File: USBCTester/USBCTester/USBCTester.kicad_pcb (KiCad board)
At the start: 4 copper layers, 114.9 x 92.1 mm, 64 parts, among them J1 AUSB1-DFN-PTR3, J2 AUSB1-DFN-PTR3, SW1 SW_Push, U1 74HC595, U2 74HC595, U3 74HC595, U4 74HC595, U5 74HC595, U6 74HC595, U7 RaspberryPi_Pico

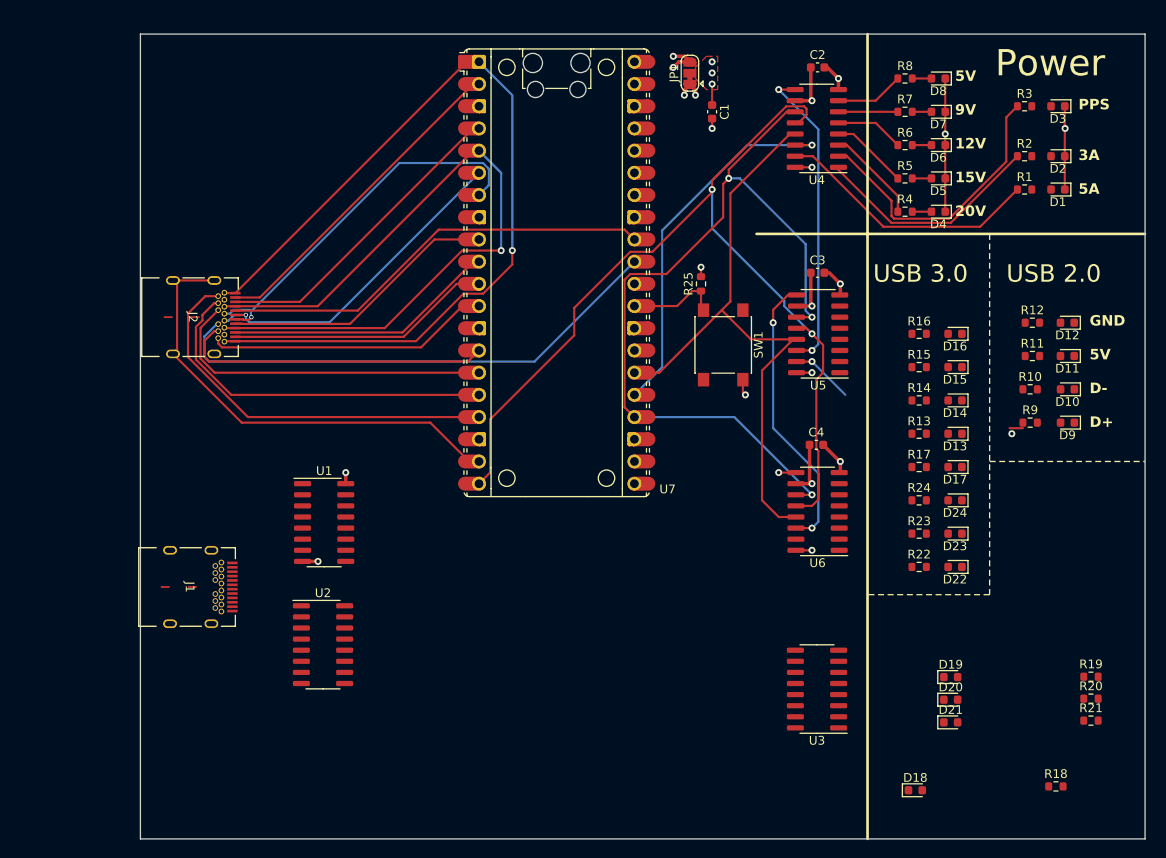
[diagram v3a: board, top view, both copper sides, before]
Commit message: add more leds and route almost everything
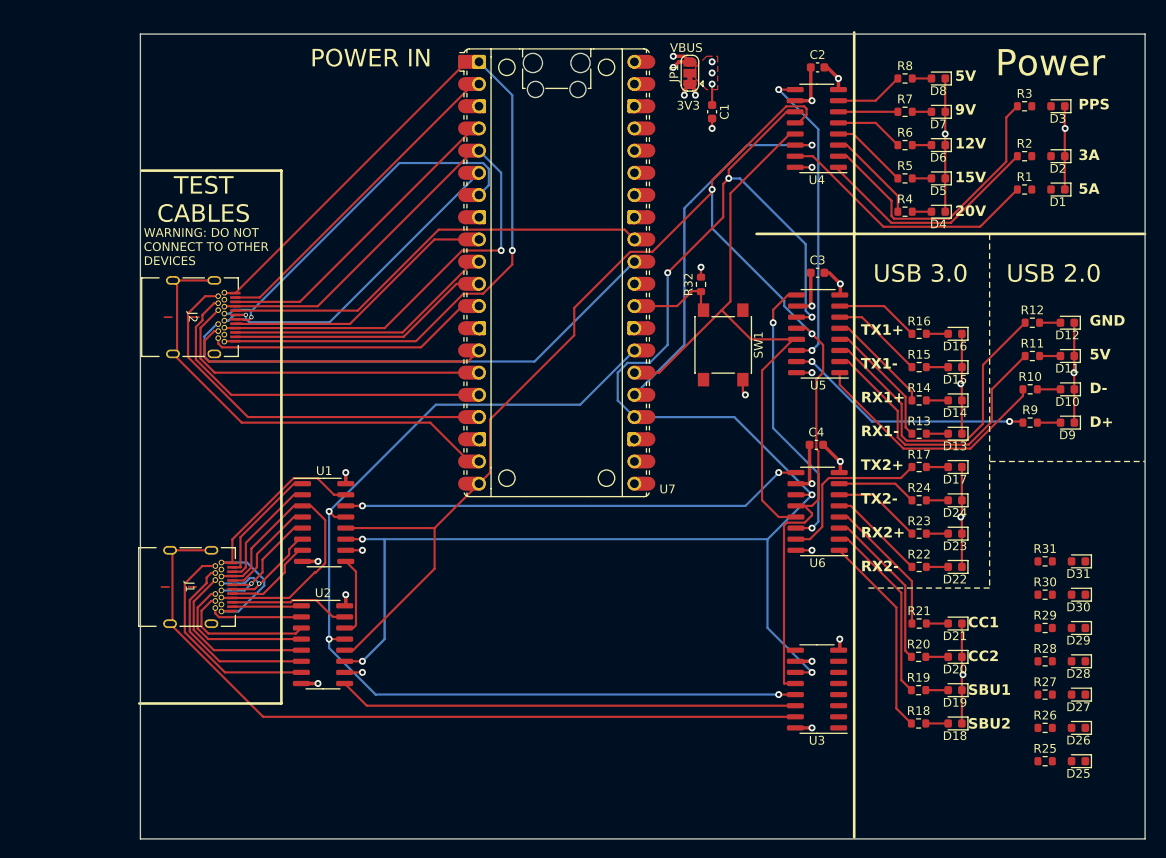
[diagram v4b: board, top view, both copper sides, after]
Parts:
- added D25: LED, LED_SMD:LED_0603_1608Metric, F.Cu at (212.1, 144.8)
- added D26: LED, LED_SMD:LED_0603_1608Metric, F.Cu at (212.1, 141.0)
- added D27: LED, LED_SMD:LED_0603_1608Metric, F.Cu at (212.1, 137.2)
- added D28: LED, LED_SMD:LED_0603_1608Metric, F.Cu at (212.1, 133.3)
- added D29: LED, LED_SMD:LED_0603_1608Metric, F.Cu at (212.1, 129.5)
- added D30: LED, LED_SMD:LED_0603_1608Metric, F.Cu at (212.1, 125.7)
- added D31: LED, LED_SMD:LED_0603_1608Metric, F.Cu at (212.1, 121.9)
- added R26: R, Resistor_SMD:R_0603_1608Metric, F.Cu at (208.3, 141.0)
- added R27: R, Resistor_SMD:R_0603_1608Metric, F.Cu at (208.3, 137.2)
- added R28: R, Resistor_SMD:R_0603_1608Metric, F.Cu at (208.3, 133.3)
- added R29: R, Resistor_SMD:R_0603_1608Metric, F.Cu at (208.3, 129.5)
- added R30: R, Resistor_SMD:R_0603_1608Metric, F.Cu at (208.3, 125.7)
- added R31: R, Resistor_SMD:R_0603_1608Metric, F.Cu at (208.3, 121.9)
- added R32: R, Resistor_SMD:R_0603_1608Metric, F.Cu at (168.9, 90.2)
- moved R25 67.3 mm to (208.3, 144.8), turned to 0 degrees
- moved R21 22.6 mm to (193.9, 129.0)
- moved R20 20.3 mm to (193.8, 132.8)
- moved R19 19.8 mm to (193.8, 136.7)
- moved R18 17.3 mm to (193.8, 140.5)
- moved D21 11.3 mm to (198.0, 129.0), turned to 180 degrees
- moved D18 8.89 mm to (198.0, 140.5), turned to 180 degrees
- moved D20 4.93 mm to (198.0, 132.8), turned to 180 degrees
- moved D19 1.57 mm to (198.0, 136.7), turned to 180 degrees
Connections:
- R25 pad 1: Net-(U7-GPIO22) -> Net-(U3-QB)
- R25 pad 2: GND -> Net-(D25-A)
- U3 pad 1: Net-(J5-Pin_2) -> Net-(U3-QB)
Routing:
- net Net-(U1-~{OE}): track 0.00 -> 117.7 mm, vias 0 -> 3
- net SRCLK: track 94.7 -> 186.3 mm, vias 3 -> 7
- net Net-(U3-QA): track 0.00 -> 89.3 mm
- net RCLK: track 110.4 -> 172.0 mm
- net Net-(U2-QH'): track 0.00 -> 52.6 mm
- net Net-(U1-SER): track 1.97 -> 53.1 mm, vias 1 -> 2
- net GND: track 39.9 -> 89.2 mm, vias 8 -> 14
- net Net-(U5-QD): track 0.00 -> 37.2 mm
- net TEST_CABLE_VBUS: track 0.00 -> 35.6 mm
- net TEST_CABLE_GROUND: track 0.00 -> 34.4 mm
- net Net-(U5-QC): track 0.00 -> 33.3 mm
- net Net-(U5-QB): track 0.00 -> 28.6 mm
- net Net-(U2-QH): track 0.00 -> 25.1 mm
- net Net-(U6-QB): track 0.00 -> 23.2 mm
- net Net-(U2-QG): track 0.00 -> 22.4 mm
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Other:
- board text added: "3V3"
- board text added: "CC1 CC2 SBU1 SBU2"
- board text added: "POWER IN"
- board text added: "TEST CABLES"
- board text added: "TX1+ TX1- RX1+ RX1- TX2+ TX2- RX2+ RX2-"
- board text added: "VBUS"
- board text added: "WARNING: DO NOT CONNECT TO OTHER DEVICES"

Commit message: label all LEDs
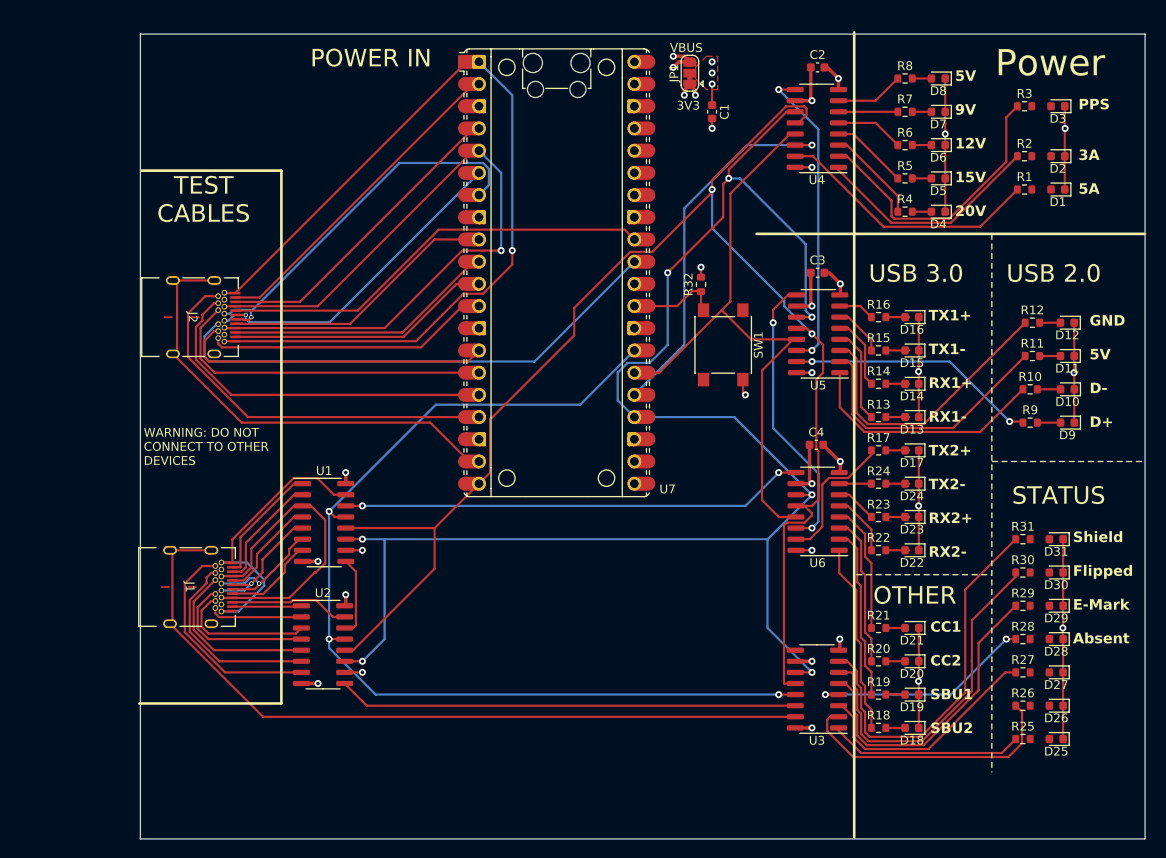
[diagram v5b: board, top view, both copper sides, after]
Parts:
- moved D13 5.28 mm to (193.0, 105.4)
- moved D14 5.28 mm to (193.0, 101.6)
- moved D16 5.28 mm to (193.0, 94.0)
- moved D17 5.28 mm to (193.0, 109.2)
- moved D22 5.28 mm to (193.0, 120.7)
- moved D23 5.28 mm to (193.0, 116.8)
- moved D24 5.28 mm to (193.0, 113.0)
- moved D15 5.28 mm to (193.0, 97.8)
- moved R13 5.01 mm to (189.2, 105.4)
- moved R14 5.01 mm to (189.2, 101.6)
- moved R16 5.01 mm to (189.2, 94.0)
- moved R17 5.01 mm to (189.2, 109.2)
- moved R22 5.01 mm to (189.2, 120.7)
- moved R23 5.01 mm to (189.2, 116.8)
- moved R24 5.01 mm to (189.2, 113.0)
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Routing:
- net Net-(U3-QH): track 0.00 -> 43.6 mm
- net Net-(U3-QG): track 0.00 -> 40.1 mm
- net Net-(U3-QF): track 0.00 -> 35.6 mm
- net Net-(U3-QC): track 0.00 -> 31.5 mm
- net Net-(U3-QD): track 0.00 -> 27.3 mm
- net Net-(U3-QE): track 0.00 -> 26.1 mm, vias 0 -> 2
- net GND: track 89.2 -> 111.8 mm, vias 14 -> 15
- net Net-(U3-QB): track 0.00 -> 22.3 mm
- net Net-(U5-QH): track 9.57 -> 4.15 mm
- net Net-(U6-QH): track 9.11 -> 3.69 mm
- net Net-(U6-QG): track 10.2 -> 4.74 mm
- net Net-(U5-QG): track 10.6 -> 5.88 mm
- net Net-(U6-QF): track 11.2 -> 7.18 mm
- net Net-(U5-QD): track 37.2 -> 33.1 mm
- net Net-(U5-QE): track 14.8 -> 11.0 mm
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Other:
- board text added: "OTHER"
- board text added: "STATUS"
- board text added: "Shield Flipped E-Mark Absent"

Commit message: add breakout pins for prototyping
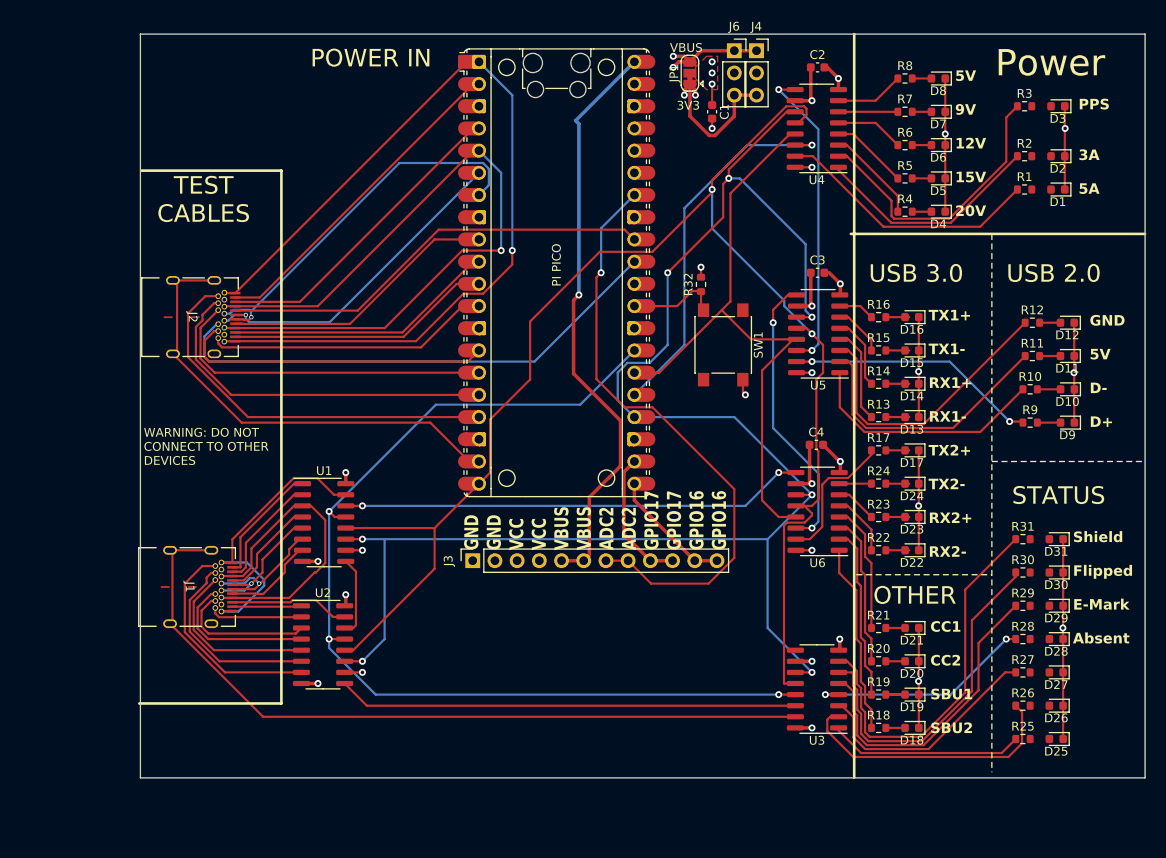
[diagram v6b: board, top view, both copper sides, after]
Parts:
- added J3: Conn_01x12, Connector_PinSocket_2.54mm:PinSocket_1x12_P2.54mm_Vertical, F.Cu at (142.8, 121.8)
- added J4: Conn_01x03, Connector_PinSocket_2.54mm:PinSocket_1x03_P2.54mm_Vertical, F.Cu at (175.3, 63.5)
- added J6: Conn_01x03, Connector_PinSocket_2.54mm:PinSocket_1x03_P2.54mm_Vertical, F.Cu at (172.7, 63.5)
- PI PICO: renamed from U7
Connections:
- PI PICO pad 21: unconnected-(U7-GPIO16-Pad21) -> GPIO16
- PI PICO pad 22: unconnected-(U7-GPIO17-Pad22) -> GPIO17
- PI PICO pad 34: unconnected-(U7-GPIO28_ADC2-Pad34) -> GPIO28
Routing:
- net VBUS: track 4.34 -> 79.2 mm, vias 2 -> 3
- net GPIO28: track 0.00 -> 68.7 mm, vias 0 -> 1
- net GPIO17: track 0.00 -> 15.6 mm
- net +3V3: track 2.95 -> 18.4 mm
- net GPIO16: track 0.00 -> 14.2 mm
- net RCLK: track 172.0 -> 174.0 mm
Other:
- board size 114.9 x 92.1 mm -> 114.9 x 85.1 mm
- board text added: "GND GND VCC VCC VBUS VBUS ADC2 ADC2 GPIO17 GPIO17 GPIO16 GPIO16"
- board text added: "TODO ADD PROTOBOARD SPACE HERE. MAYBE ALSO POT FOOTPRINT FOR VOLTAGE SELECTION RESOLVE DRC ERRORS"
- board text removed: "TODO: add more LEDs for U3, to indicate CC/VCON status details and whether cable is reversed/absent"

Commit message: made board more compact
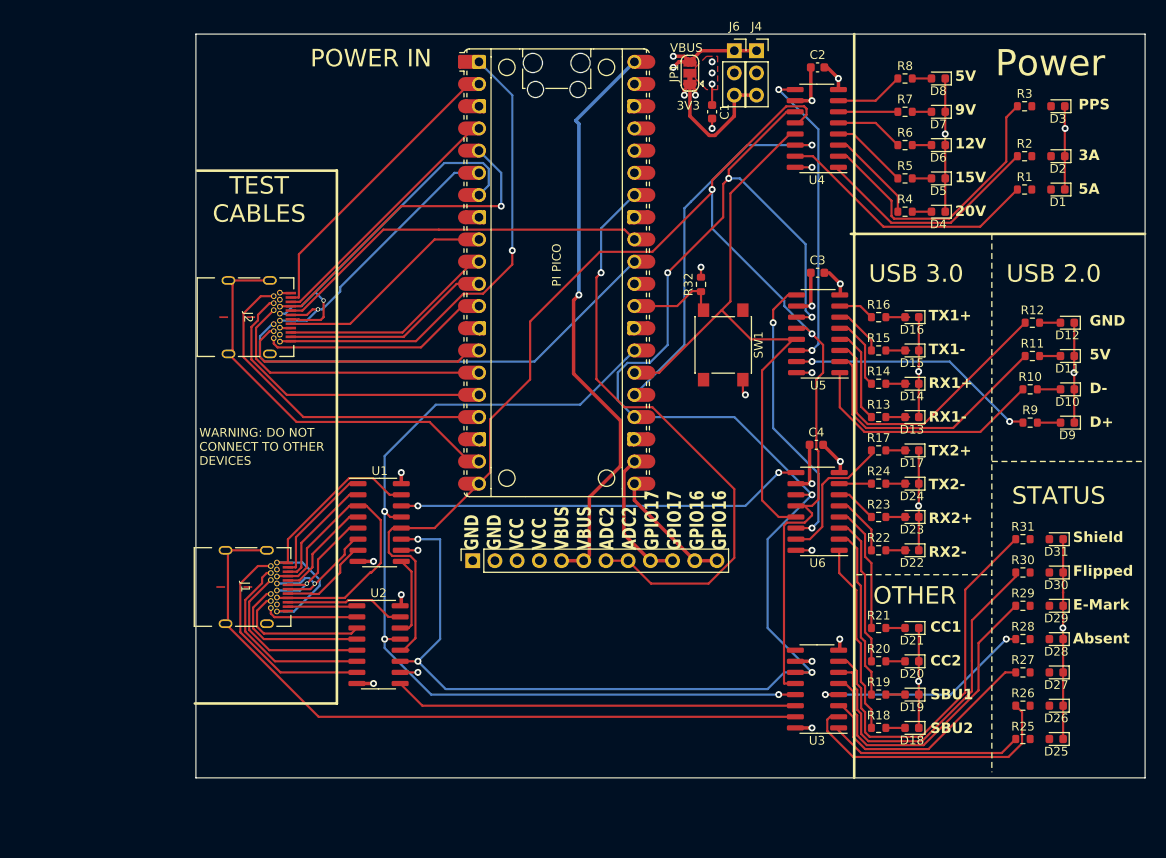
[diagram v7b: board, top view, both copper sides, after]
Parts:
- moved J1 6.35 mm to (116.5, 124.8)
- moved U1 6.35 mm to (132.1, 117.5)
- moved J2 6.35 mm to (116.8, 94.0)
- moved U2 6.35 mm to (132.0, 131.4)
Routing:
- net TEST_CABLE_VBUS_IN: track 84.4 -> 39.4 mm
- net TEST_CABLE_GROUND_IN: track 101.5 -> 57.7 mm
- net Net-(U1-~{OE}): track 117.7 -> 108.7 mm
- net Net-(U7-GPIO6): track 32.7 -> 25.5 mm
- net Net-(U7-GPIO14): track 53.6 -> 47.3 mm
- net Net-(U2-QH'): track 52.6 -> 46.3 mm
- net Net-(U7-GPIO8): track 30.4 -> 24.0 mm
- net Net-(U7-GPIO7): track 31.2 -> 24.9 mm
- net Net-(U7-GPIO2): track 36.1 -> 29.7 mm
- net Net-(U7-GPIO27_ADC1): track 50.0 -> 43.6 mm
- net Net-(U7-GPIO26_ADC0): track 58.6 -> 52.3 mm
- net Net-(U7-GPIO12): track 41.8 -> 35.5 mm
- net Net-(U7-GPIO11): track 38.9 -> 32.5 mm
- net Net-(U7-GPIO10): track 36.0 -> 29.7 mm
- net Net-(U1-SER): track 53.1 -> 46.7 mm
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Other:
- board size 114.9 x 85.1 mm -> 108.6 x 85.1 mm
- board text added: "TODO ADD PROTOBOARD SPACE HERE. MAYBE ALSO POT FOOTPRINT FOR VOLTAGE SELECTION RESOLVE DRC ERRORS ADD NAME, REV, ETC"
- board text removed: "TODO ADD PROTOBOARD SPACE HERE. MAYBE ALSO POT FOOTPRINT FOR VOLTAGE SELECTION RESOLVE DRC ERRORS"

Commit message: add 3rd incompatible footprint design
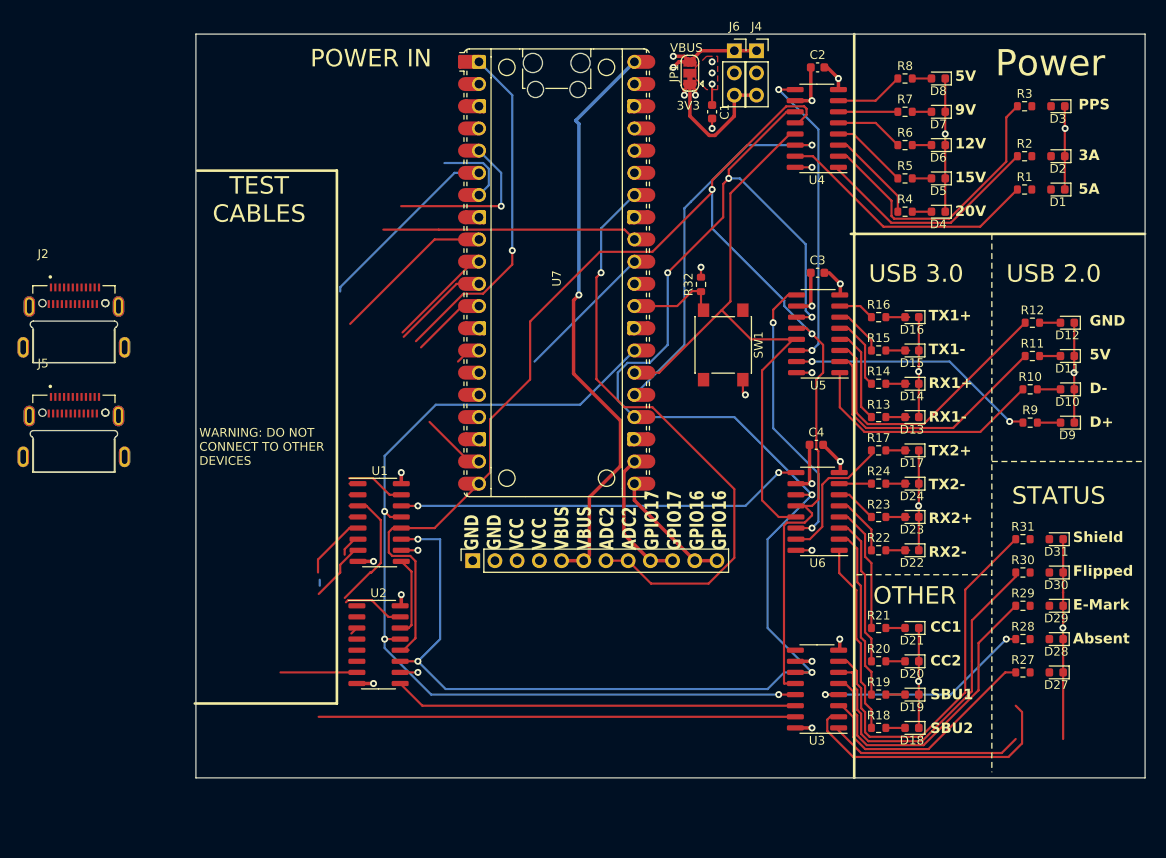
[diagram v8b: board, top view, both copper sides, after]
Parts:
- removed D25, D26: LED, LED_SMD:LED_0603_1608Metric
- removed J1: AUSB1-DFN-PTR3, USBCFootprint:USBCConnector_WithShield
- removed R25, R26: R, Resistor_SMD:R_0603_1608Metric
- added J5: 2388749-1, USBCFootprint:USBC2, F.Cu at (97.2, 104.9)
- J2: value AUSB1-DFN-PTR3 -> 2388749-1; footprint USBCFootprint:USBCConnector_WithShield -> USBCFootprint:USBC2
- U7: renamed from PI PICO
- moved J2 19.7 mm to (97.2, 92.4), turned to 0 degrees
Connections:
- net TEST_CABLE_VBUS_IN renamed Net-(U7-GPIO3)
- J2 pad A1: TEST_CABLE_GROUND_IN -> Net-(U7-GPIO11)
- J2 pad A10: Net-(U7-GPIO7) -> Net-(J2-SSRXN2)
- J2 pad A11: Net-(U7-GPIO8) -> Net-(J2-SSRXP2)
- J2 pad A12: TEST_CABLE_GROUND_IN -> Net-(U7-GPIO11)
- J2 pad A2: Net-(U7-GPIO1) -> Net-(J2-SSTXP1)
- J2 pad A3: Net-(U7-GPIO2) -> Net-(J2-SSTXN1)
- J2 pad A5: Net-(U7-GPIO27_ADC1) -> Net-(J2-CC1)
- J2 pad A6: TEST_CABLE_D+_IN -> Net-(J2-DP1)
- J2 pad A7: TEST_CABLE_D-_IN -> Net-(J2-DN1)
- J2 pad A8: Net-(U7-GPIO6) -> Net-(J2-SBU1)
- J2 pad B1: TEST_CABLE_GROUND_IN -> Net-(U7-GPIO11)
- J2 pad B10: Net-(U7-GPIO12) -> Net-(J2-SSRXN1)
- J2 pad B11: Net-(U7-GPIO13) -> Net-(J2-SSRXP1)
- J2 pad B12: TEST_CABLE_GROUND_IN -> Net-(U7-GPIO11)
- J2 pad B2: Net-(U7-GPIO9) -> Net-(J2-SSTXP2)
- J2 pad B3: Net-(U7-GPIO10) -> Net-(J2-SSTXN2)
- J2 pad B5: Net-(U7-GPIO26_ADC0) -> Net-(J2-CC2)
- J2 pad B6: TEST_CABLE_D+_IN -> Net-(J2-DP1)
- J2 pad B7: TEST_CABLE_D-_IN -> Net-(J2-DN1)
- J2 pad B8: Net-(U7-GPIO11) -> Net-(J2-SBU2)
- U1 pad 14: Net-(U1-SER) -> unconnected-(U1-SER-Pad14)
- U1 pad 15: TEST_CABLE_GROUND -> Net-(J5-DN2)
- U1 pad 3: TEST_CABLE_VBUS -> Net-(J5-SSRXP1)
- U1 pad 5: TEST_CABLE_D+ -> Net-(J5-SSTXP1)
- U1 pad 6: TEST_CABLE_D- -> Net-(J5-SSTXN1)
- U6 pad 9: Net-(U1-SER) -> unconnected-(U6-QH'-Pad9)
- U7 pad 1: TEST_CABLE_GROUND_IN -> Net-(J2-SBU2)
- U7 pad 10: Net-(U7-GPIO7) -> Net-(J2-DN1)
- U7 pad 11: Net-(U7-GPIO8) -> Net-(J2-SBU1)
- U7 pad 12: Net-(U7-GPIO9) -> Net-(J2-SSRXN2)
- U7 pad 14: Net-(U7-GPIO10) -> Net-(J2-SSRXP2)
- U7 pad 16: Net-(U7-GPIO12) -> Net-(J2-SSTXP2)
- U7 pad 17: Net-(U7-GPIO13) -> Net-(J2-SSTXN2)
- U7 pad 2: Net-(U7-GPIO1) -> Net-(J2-SSRXN1)
- U7 pad 31: Net-(U7-GPIO26_ADC0) -> Net-(J2-CC1)
- U7 pad 32: Net-(U7-GPIO27_ADC1) -> Net-(J2-CC2)
- U7 pad 4: Net-(U7-GPIO2) -> Net-(J2-SSRXP1)
- U7 pad 6: TEST_CABLE_D+_IN -> Net-(J2-SSTXP1)
- U7 pad 7: TEST_CABLE_D-_IN -> Net-(J2-SSTXN1)
- U7 pad 9: Net-(U7-GPIO6) -> Net-(J2-DP1)
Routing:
- net TEST_CABLE_GROUND_IN: track 57.7 -> 0.00 mm, vias 1 -> 0
- net Net-(U7-GPIO26_ADC0): track 52.3 -> 0.00 mm
- net (no net): track 0.00 -> 47.4 mm, vias 0 -> 2
- net Net-(U1-SER): track 46.7 -> 0.00 mm, vias 2 -> 0
- net Net-(U7-GPIO27_ADC1): track 43.6 -> 0.00 mm
- net TEST_CABLE_D-_IN: track 42.0 -> 0.00 mm, vias 1 -> 0
- net Net-(J2-SBU2): track 0.00 -> 40.8 mm, vias 0 -> 1
- net Net-(U7-GPIO14): track 47.3 -> 7.53 mm
- net Net-(U7-GPIO13): track 39.0 -> 0.00 mm
- net TEST_CABLE_VBUS: track 35.6 -> 0.00 mm
- net Net-(U7-GPIO12): track 35.5 -> 0.00 mm
- net Net-(U7-GPIO1): track 34.5 -> 0.00 mm
- net TEST_CABLE_GROUND: track 34.4 -> 0.00 mm
- net TEST_CABLE_D+_IN: track 33.4 -> 0.00 mm, vias 1 -> 0
- net Net-(U7-GPIO11): track 32.5 -> 0.00 mm
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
